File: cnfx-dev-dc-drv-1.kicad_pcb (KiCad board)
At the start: 2 copper layers, 0 parts

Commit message: pcb: import footprints from schem
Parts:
- added C1: 1u, Capacitor_SMD:C_0402_1005Metric, F.Cu at (84.7, 127.7)
- added C10: 20p, Capacitor_SMD:C_0603_1608Metric, F.Cu at (93.8, 145.4)
- added C11: 0u1, Capacitor_SMD:C_0402_1005Metric, F.Cu at (87.6, 129.7)
- added C12: 0u1, Capacitor_SMD:C_0402_1005Metric, F.Cu at (87.6, 131.6)
- added C13: 10u, Capacitor_SMD:C_0805_2012Metric, F.Cu at (94.1, 134.2)
- added C14: 0u1, Capacitor_SMD:C_0402_1005Metric, F.Cu at (87.6, 133.6)
- added C15: 0u1, Capacitor_SMD:C_0402_1005Metric, F.Cu at (87.6, 135.6)
- added C16: 1u, Capacitor_SMD:C_0402_1005Metric, F.Cu at (90.5, 127.7)
- added C17: 1u, Capacitor_SMD:C_0402_1005Metric, F.Cu at (90.5, 129.7)
- added C18: 10n, Capacitor_SMD:C_0402_1005Metric, F.Cu at (90.5, 131.6)
- added C19: 0u1, Capacitor_SMD:C_0402_1005Metric, F.Cu at (87.7, 152.7)
- added C2: 0u1, Capacitor_SMD:C_0402_1005Metric, F.Cu at (84.7, 129.7)
- added C20: 22u, Capacitor_SMD:C_0402_1005Metric, F.Cu at (87.7, 154.7)
- added C21: 22u, Capacitor_SMD:C_0402_1005Metric, F.Cu at (87.7, 156.7)
- added C22: 0u1, Capacitor_SMD:C_0402_1005Metric, F.Cu at (73.4, 152.7)
- added C23: 22u, Capacitor_SMD:C_0402_1005Metric, F.Cu at (73.4, 154.7)
- added C24: 22u, Capacitor_SMD:C_0402_1005Metric, F.Cu at (73.4, 156.7)
- added C3: C, Capacitor_SMD:C_0402_1005Metric, F.Cu at (84.7, 131.6)
- added C4: 1n, Capacitor_SMD:C_0402_1005Metric, F.Cu at (84.7, 133.6)
- added C5: 22u, Capacitor_SMD:C_0402_1005Metric, F.Cu at (84.7, 135.6)
- added C6: 10u, Capacitor_SMD:C_0805_2012Metric, F.Cu at (94.1, 128.2)
- added C7: 0u1, Capacitor_SMD:C_0402_1005Metric, F.Cu at (87.6, 127.7)
- added C8: 10u, Capacitor_SMD:C_0805_2012Metric, F.Cu at (94.1, 131.2)
- added C9: 20p, Capacitor_SMD:C_0603_1608Metric, F.Cu at (93.8, 142.9)
- added D1: WS2812B, LED_SMD:LED_WS2812B_PLCC4_5.0x5.0mm_P3.2mm, F.Cu at (87.4, 146.4)
- added D2: H5VU10U, GLCS:Diode_DFN1006, F.Cu at (73.6, 139.1)
- added D3: H5VU10U, GLCS:Diode_DFN1006, F.Cu at (73.6, 141.0)
- added D4: H5VU10U, GLCS:Diode_DFN1006, F.Cu at (73.6, 143.0)
- added D5: H5VU10U, GLCS:Diode_DFN1006, F.Cu at (73.6, 145.0)
- added D6: GREEN, LED_SMD:LED_0805_2012Metric, F.Cu at (98.6, 128.2)
- added D7: H5VU10U, GLCS:Diode_DFN1006, F.Cu at (73.6, 147.0)
- added D8: YELLOW, LED_SMD:LED_0805_2012Metric, F.Cu at (98.6, 131.3)
- added FB1: 600Ω@100M, Inductor_SMD:L_0805_2012Metric, F.Cu at (93.1, 123.7)
- added J1: Conn_01x03, Connector_JST:JST_XH_B3B-XH-A_1x03_P2.50mm_Vertical, F.Cu at (88.7, 117.9)
- added J2: TC2030, Connector:Tag-Connect_TC2030-IDC-NL_2x03_P1.27mm_Vertical, F.Cu at (95.8, 139.1)
- added J3: Conn_01x02, Connector_JST:JST_XH_B2B-XH-A_1x02_P2.50mm_Vertical, F.Cu at (66.0, 117.9)
- added J4: Conn_01x02, Connector_JST:JST_XH_B2B-XH-A_1x02_P2.50mm_Vertical, F.Cu at (66.0, 125.7)
- added J5: Conn_01x04_Pin, Connector_PinHeader_2.54mm:PinHeader_1x04_P2.54mm_Vertical, F.Cu at (74.2, 116.8)
- added J6: Conn_01x04_Pin, Connector_PinHeader_2.54mm:PinHeader_1x04_P2.54mm_Vertical, F.Cu at (78.8, 116.8)
- added J7: Conn_01x02, Connector_JST:JST_XH_B2B-XH-A_1x02_P2.50mm_Vertical, F.Cu at (80.3, 155.1)
- added J8: Conn_01x02, Connector_JST:JST_XH_B2B-XH-A_1x02_P2.50mm_Vertical, F.Cu at (66.0, 155.1)
- added JP1: Jumper_2_Small_Bridged, Jumper:SolderJumper-2_P1.3mm_Open_RoundedPad1.0x1.5mm, F.Cu at (98.5, 134.6)
- added R1: 120, Resistor_SMD:R_1206_3216Metric, F.Cu at (88.0, 124.0)
- added R2: 820, Resistor_SMD:R_0402_1005Metric, F.Cu at (98.6, 115.5)
- added R3: 5k1, Resistor_SMD:R_0402_1005Metric, F.Cu at (98.6, 117.5)
- added R4: 10k, Resistor_SMD:R_0402_1005Metric, F.Cu at (98.6, 119.5)
- added R5: 5k1, Resistor_SMD:R_0402_1005Metric, F.Cu at (98.6, 121.5)
- added R6: 10k, Resistor_SMD:R_0402_1005Metric, F.Cu at (98.6, 123.5)
- added R7: 560, Resistor_SMD:R_0603_1608Metric, F.Cu at (93.8, 147.9)
- added R8: 5k1, Resistor_SMD:R_0402_1005Metric, F.Cu at (98.6, 125.4)
- added SW1: SW_Push, Button_Switch_SMD:SW_SPST_TS-1088-xR020, F.Cu at (66.0, 132.4)
- added SW2: SW_Push, Button_Switch_SMD:SW_SPST_TS-1088-xR020, F.Cu at (66.0, 136.9)
- added SW3: SW_Push, Button_Switch_SMD:SW_SPST_TS-1088-xR020, F.Cu at (66.0, 141.5)
- added TP1: TestPoint, GLCS:TestPoint_Keystone_5015_Micro_Mini, F.Cu at (98.4, 143.5)
- added TP2: TestPoint, GLCS:TestPoint_Keystone_5015_Micro_Mini, F.Cu at (98.4, 147.2)
- added TP3: TestPoint, TestPoint:TestPoint_Pad_D2.0mm, F.Cu at (83.2, 116.5)
- added TP4: TestPoint, TestPoint:TestPoint_Pad_D2.0mm, F.Cu at (83.2, 120.6)
- added TP5: TestPoint, TestPoint:TestPoint_Pad_D2.0mm, F.Cu at (83.2, 124.6)
- added U1: SN65HVD230, Package_SO:SOIC-8_3.9x4.9mm_P1.27mm, F.Cu at (87.5, 139.9)
- added U2: TPS259472A, GLCS:Texas_RPW0010A_VQFN-HR-10_2x2mm_P0.5mm, F.Cu at (64.6, 145.8)
- added U3: HT753-1, Package_TO_SOT_SMD:SOT-89-3, F.Cu at (78.4, 146.4)
- added U4: STM32F103C8Tx, Package_QFP:LQFP-48_7x7mm_P0.5mm, F.Cu at (77.6, 132.4)
- added U5: DRV8837, Package_SON:WSON-8-1EP_2x2mm_P0.5mm_EP0.9x1.6mm, F.Cu at (79.0, 161.5)
- added U6: DRV8837, Package_SON:WSON-8-1EP_2x2mm_P0.5mm_EP0.9x1.6mm, F.Cu at (64.7, 161.5)
- added Y1: 8M, Crystal:Crystal_SMD_5032-2Pin_5.0x3.2mm, F.Cu at (78.7, 140.7)

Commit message: schem: remove extra gpios
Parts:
- removed J5: Conn_01x04_Pin, Connector_PinHeader_2.54mm:PinHeader_1x04_P2.54mm_Vertical
- moved R2 85.3 mm to (32.7, 169.7)
- moved R3 85.3 mm to (32.7, 171.6)
- moved R4 85.3 mm to (32.7, 173.6)
- moved R5 85.3 mm to (32.7, 175.6)
- moved D6 78.3 mm to (41.8, 182.1)
- moved J1 74.4 mm to (37.6, 172.0)
- moved C1 72.1 mm to (32.7, 177.6)
- moved TP1 70.8 mm to (36.8, 178.3)
- moved TP2 70.8 mm to (36.8, 182.1)
- moved C3 70.8 mm to (32.7, 179.6)
- moved C4 70.8 mm to (32.7, 181.5)
- moved C5 70.8 mm to (32.7, 183.5)
- moved U6 67.2 mm to (130.5, 147.8)
- moved C22 67.2 mm to (139.2, 139.1)
- moved C23 67.2 mm to (139.2, 141.1)
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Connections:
- U4 pad 21: Net-(J5-Pin_3) -> unconnected-(U4-PB10-Pad21)
- U4 pad 22: Net-(J5-Pin_4) -> unconnected-(U4-PB11-Pad22)
- U4 pad 45: Net-(J5-Pin_1) -> unconnected-(U4-PB8-Pad45)
- U4 pad 46: Net-(J5-Pin_2) -> unconnected-(U4-PB9-Pad46)

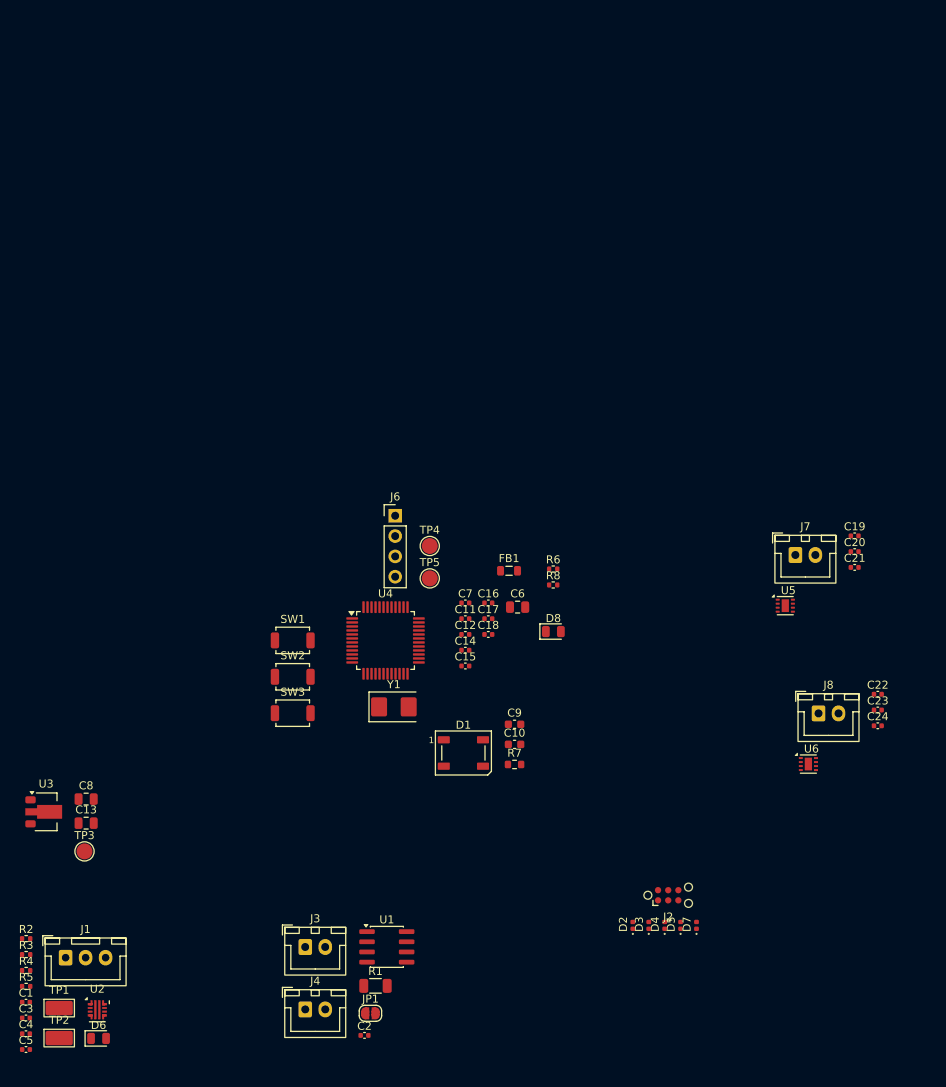
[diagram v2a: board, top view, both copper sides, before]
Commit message: pcb: add initial layout
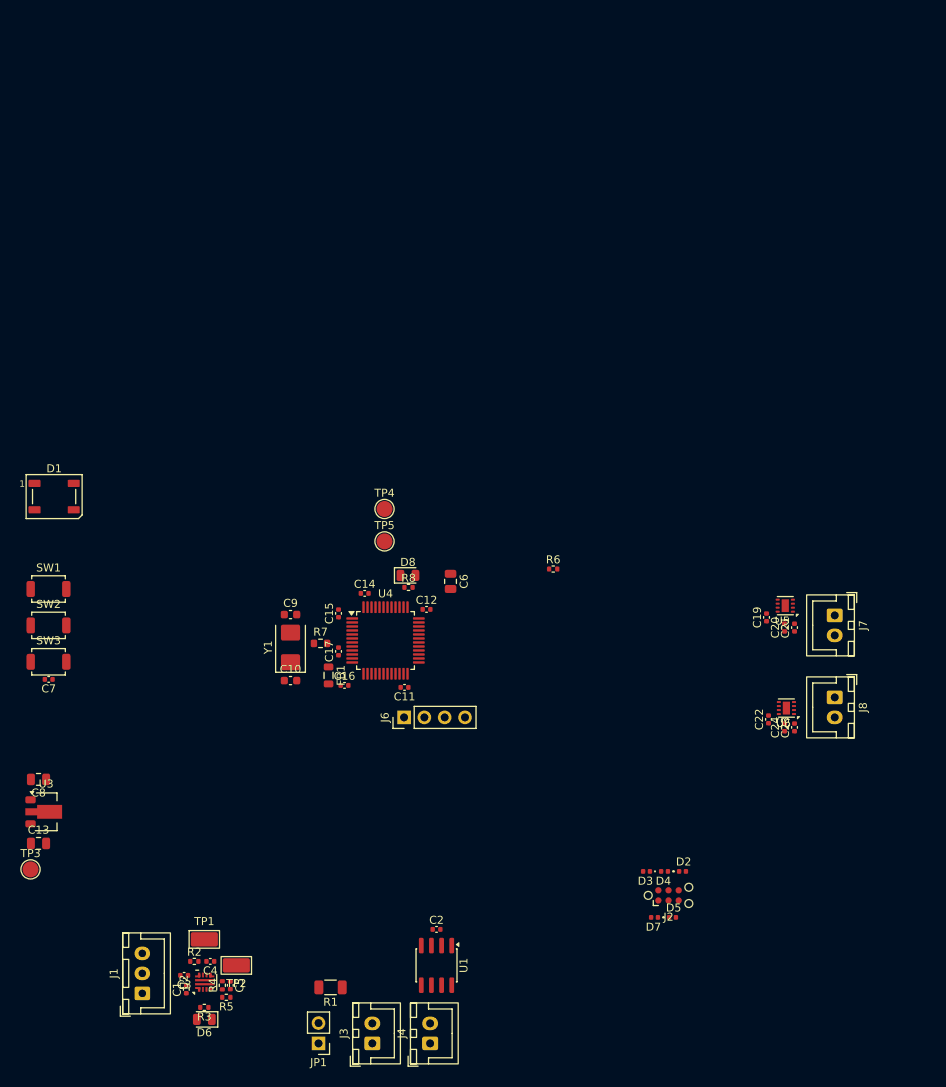
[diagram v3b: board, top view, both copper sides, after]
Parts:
- removed C18: 10n, Capacitor_SMD:C_0402_1005Metric
- JP1: footprint Jumper:SolderJumper-2_P1.3mm_Open_RoundedPad1.0x1.5mm -> Connector_PinHeader_2.54mm:PinHeader_1x02_P2.54mm_Vertical
- moved D1 60.4 mm to (36.2, 114.4)
- moved C7 53.0 mm to (35.5, 137.2), turned to 180 degrees
- moved SW1 31.2 mm to (35.5, 126.0)
- moved SW2 31.2 mm to (35.5, 130.5)
- moved SW3 31.2 mm to (35.5, 135.1)
- moved C9 31.2 mm to (65.8, 129.2)
- moved C10 29.1 mm to (65.8, 137.4)
- moved R7 28.6 mm to (69.5, 132.8)
- moved C5 26.8 mm to (58.2, 175.5), turned to -90 degrees
- moved FB1 26.1 mm to (70.5, 136.8), turned to -90 degrees
- moved J6 25.2 mm to (79.9, 142.0), turned to 90 degrees
- moved R5 25.1 mm to (57.7, 177.0), turned to 180 degrees
- moved C4 24.8 mm to (55.7, 172.5), turned to 180 degrees
- moved R4 24.6 mm to (57.2, 175.5), turned to 90 degrees
- moved TP2 23.9 mm to (59.0, 173.0), turned to 180 degrees
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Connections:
- R2 pad 2: Net-(U2-ILM) -> /ILM
- TP1 pad 1: Net-(U2-ILM) -> /ILM
- U2 pad 9: Net-(U2-ILM) -> /ILM
- U4 pad 18: unconnected-(U4-PB0-Pad18) -> /ILM

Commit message: pcb: refine layout
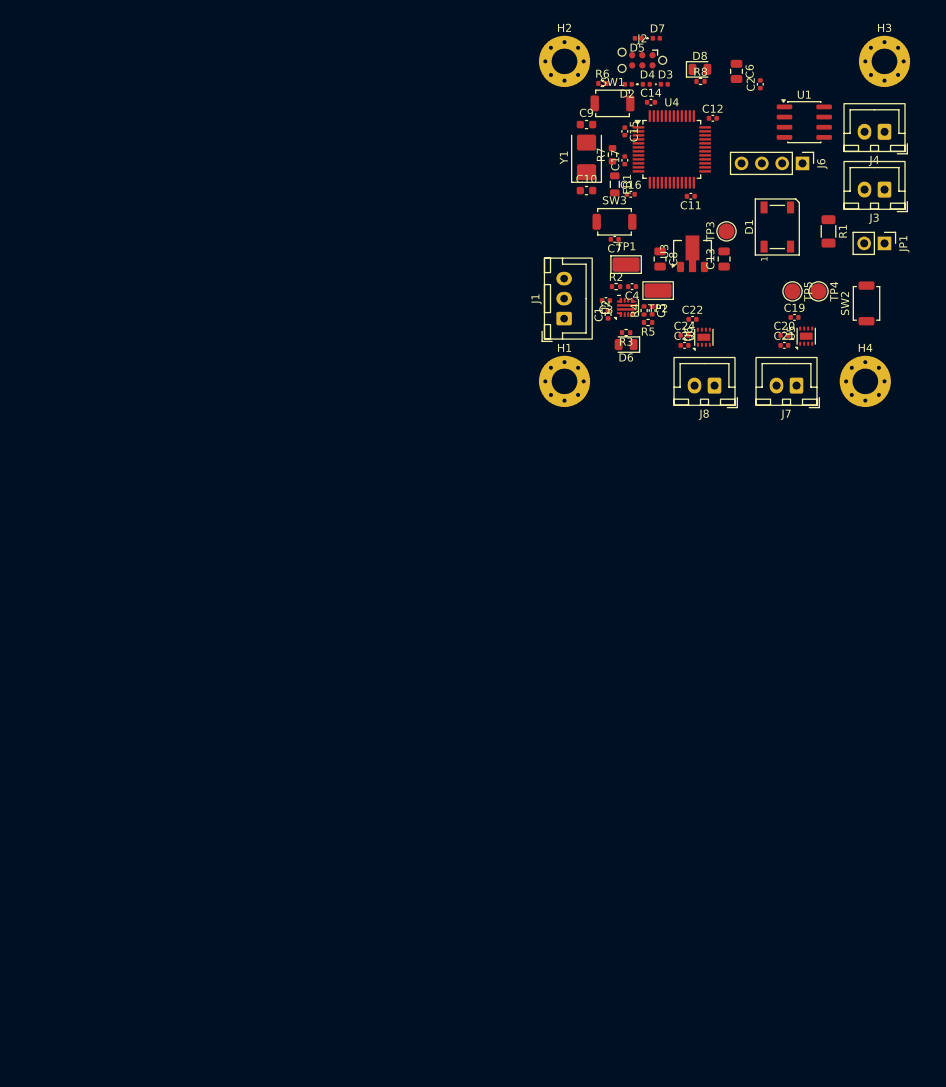
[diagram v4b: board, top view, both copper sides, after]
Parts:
- added H1: MountingHole_Pad, MountingHole:MountingHole_3.2mm_M3_Pad_Via, F.Cu at (100.0, 100.0)
- added H2: MountingHole_Pad, MountingHole:MountingHole_3.2mm_M3_Pad_Via, F.Cu at (100.0, 60.0)
- added H3: MountingHole_Pad, MountingHole:MountingHole_3.2mm_M3_Pad_Via, F.Cu at (140.0, 60.0)
- added H4: MountingHole_Pad, MountingHole:MountingHole_3.2mm_M3_Pad_Via, F.Cu at (137.6, 100.0)
- moved J4 127.3 mm to (140.0, 68.8), turned to 180 degrees
- moved J3 124.5 mm to (140.0, 76.0), turned to 180 degrees
- moved JP1 122.5 mm to (140.0, 82.8), turned to -90 degrees
- moved TP3 118.0 mm to (120.2, 81.2), turned to 90 degrees
- moved U1 115.0 mm to (130.0, 67.6), turned to 0 degrees
- moved R1 113.2 mm to (133.0, 81.2), turned to -90 degrees
- moved C2 113.1 mm to (124.5, 62.9), turned to 90 degrees
- moved C13 112.6 mm to (119.9, 84.7), turned to 90 degrees
- moved D5 110.0 mm to (109.2, 57.1), turned to 180 degrees
- moved SW2 109.9 mm to (137.8, 90.2), turned to 90 degrees
- moved D7 109.9 mm to (111.5, 57.1), turned to 0 degrees
- moved U3 106.9 mm to (116.0, 83.8), turned to 90 degrees
- moved J2 104.4 mm to (109.7, 59.9), turned to 180 degrees
- moved C8 101.3 mm to (111.9, 84.7), turned to -90 degrees
- moved C5 99.5 mm to (111.0, 91.1)
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
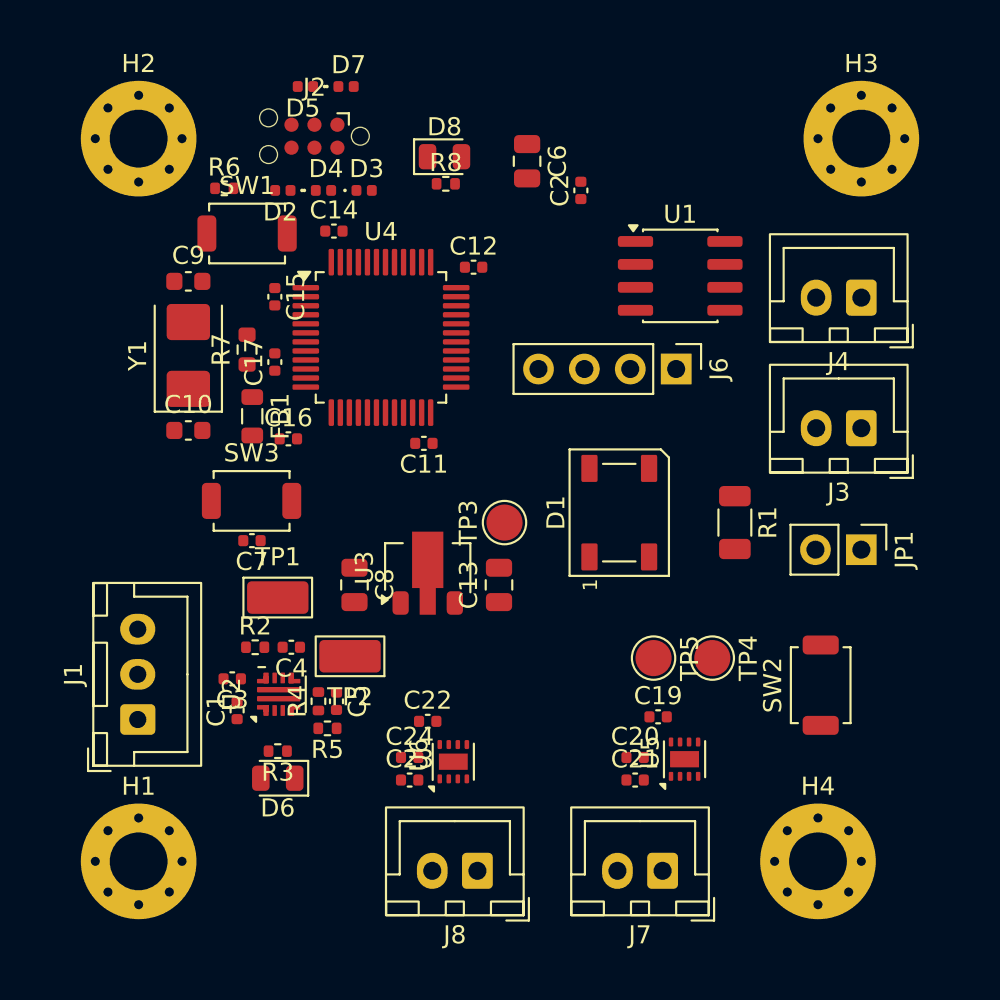
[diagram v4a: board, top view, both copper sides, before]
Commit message: pcb: add board outline
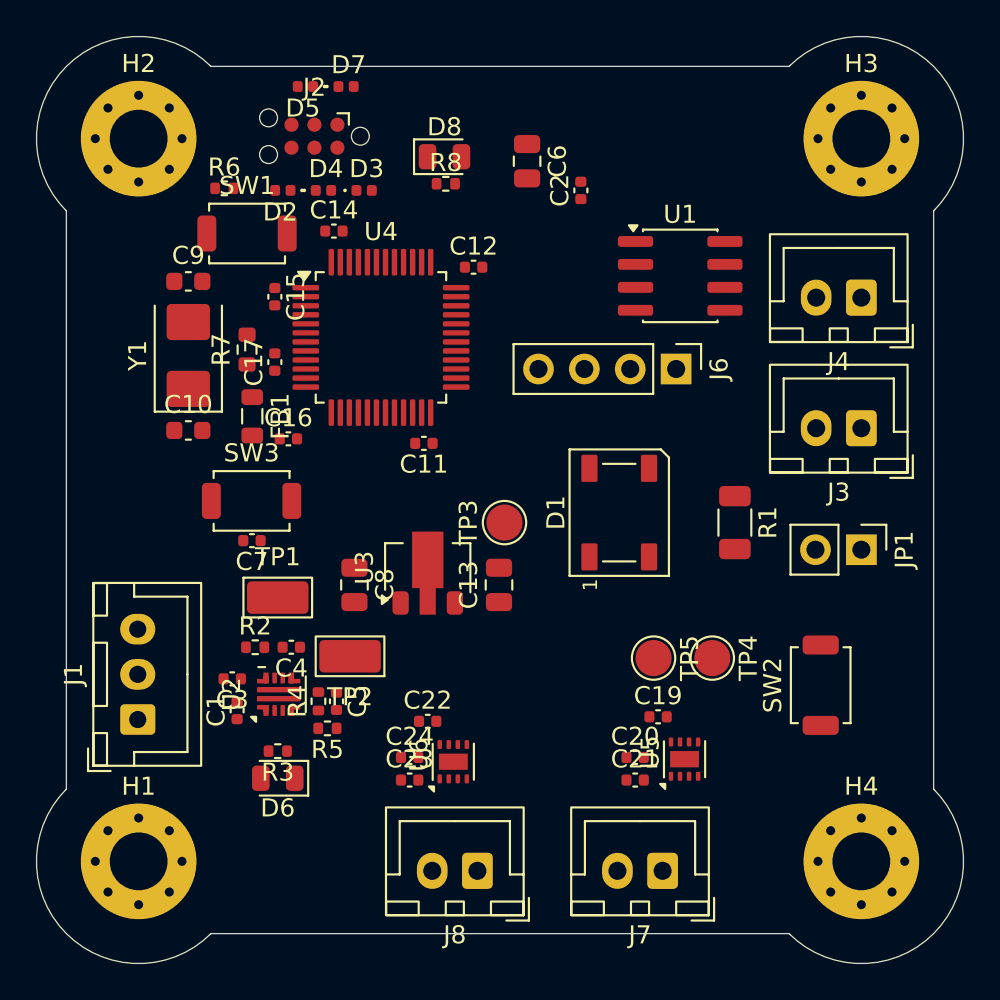
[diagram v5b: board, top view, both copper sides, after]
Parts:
- moved H4 2.40 mm to (140.0, 100.0)
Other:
- board outline added: 51.3 x 51.3 mm
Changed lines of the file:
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@@
 	(footprint "MountingHole:MountingHole_3.2mm_M3_Pad_Via"
 		(layer "F.Cu")
-		(at 137.6 100)
+		(at 140 100)
 		(descr "Mounting Hole 3.2mm, M3, generated by kicad-footprint-generator mountinghole.py")
 		(tags "mountinghole M3")
@@
 		)
 	)
+	(gr_arc
+		(start 96 64)
+		(mid 96 56)
+		(end 104 56)
+		(stroke
+			(width 0.05)
+			(type default)
+		)
+		(layer "Edge.Cuts")
+	)
+	(gr_line
+		(start 96 96)
+		(end 96 64)
+		(stroke
+			(width 0.05)
+			(type default)
+		)
+		(layer "Edge.Cuts")
+	)
+	(gr_line
+		(start 104 56)
+		(end 136 56)
+		(stroke
+			(width 0.05)
+			(type default)
+		)
+		(layer "Edge.Cuts")
+	)
+	(gr_arc
+		(start 104 104)
+		(mid 96 104)
+		(end 96 96)
+		(stroke
+			(width 0.05)
+			(type default)
+		)
+		(layer "Edge.Cuts")
+	)
+	(gr_arc
+		(start 136 56)
+		(mid 144 56)
+		(end 144 64)
+		(stroke
+			(width 0.05)
+			(type default)
+		)
+		(layer "Edge.Cuts")
+	)
+	(gr_line
+		(start 136 104)
+		(end 104 104)
+		(stroke
+			(width 0.05)
+			(type default)
+		)
+		(layer "Edge.Cuts")
+	)
+	(gr_line
+		(start 144 64)
+		(end 144 96)
+		(stroke
+			(width 0.05)
+			(type default)
+		)
+		(layer "Edge.Cuts")
+	)
+	(gr_arc
+		(start 144 96)
+		(mid 144 104)
+		(end 136 104)
+		(stroke
+			(width 0.05)
+			(type default)
+		)
+		(layer "Edge.Cuts")
+	)
 	(embedded_fonts no)
